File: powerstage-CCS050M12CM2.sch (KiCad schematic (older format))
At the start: 47 parts, among them Q2 CCS050M12CM2, U10 74LVC2G04, U11 TXS0108E

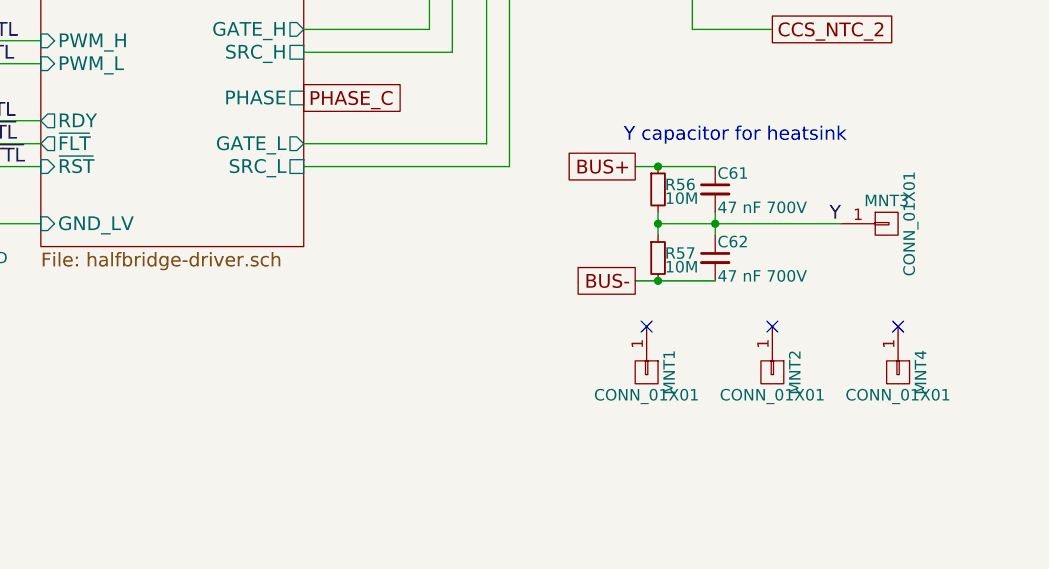
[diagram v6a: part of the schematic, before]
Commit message: YCAPS: Add real safety caps, dual Res
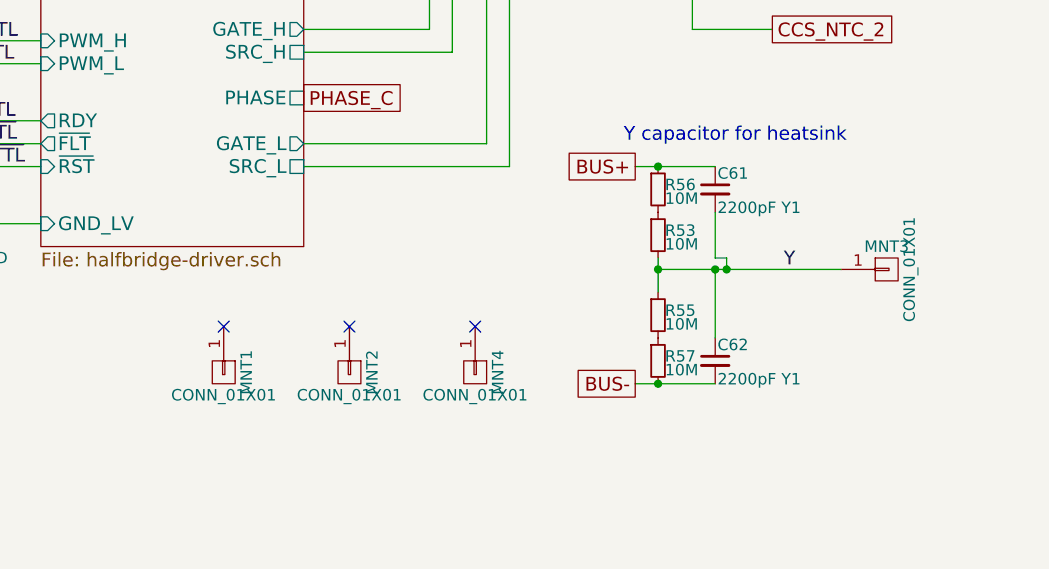
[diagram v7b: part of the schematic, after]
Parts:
- added R53, R55: 10M, Resistors_SMD:R_0805, symbol R_Small
- C61, C62: value 47 nF 700V -> 2200pF Y1; footprint Capacitors_SMD:C_1210 -> sictroller:CAP_ERP610_12-5MM; MPN (none) -> ERP610W222MERU
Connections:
- net Y: now also R53.2, R55.1; no longer R56.2, R57.1
- new net: R53.1, R56.2
- new net: R55.2, R57.1
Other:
- moved on the sheet: C62, MNT1, MNT2, MNT3, MNT4, R57
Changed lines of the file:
@@
 $EndDescr
 $Comp
-L +5VD #PWR116
+L +5VD #PWR0112
 U 1 1 57A1909B
 P 4150 4250
-F 0 "#PWR116" H 4150 4100 50  0001 C CNN
+F 0 "#PWR0112" H 4150 4100 50  0001 C CNN
 F 1 "+5VD" H 4150 4390 50  0000 C CNN
 F 2 "" H 4150 4250 50  0000 C CNN
@@
 $EndComp
 $Comp
-L GNDD #PWR111
+L GNDD #PWR0113
 U 1 1 57A19106
 P 2950 4550
-F 0 "#PWR111" H 2950 4300 50  0001 C CNN
+F 0 "#PWR0113" H 2950 4300 50  0001 C CNN
 F 1 "GNDD" H 2950 4400 50  0000 C CNN
 F 2 "" H 2950 4550 50  0000 C CNN
@@
 $EndComp
 $Comp
-L GNDD #PWR117
+L GNDD #PWR0114
 U 1 1 57A1910C
 P 4300 4550
-F 0 "#PWR117" H 4300 4300 50  0001 C CNN
+F 0 "#PWR0114" H 4300 4300 50  0001 C CNN
 F 1 "GNDD" H 4300 4400 50  0000 C CNN
 F 2 "" H 4300 4550 50  0000 C CNN
@@
 $EndComp
 $Comp
-L GNDD #PWR114
+L GNDD #PWR0115
 U 1 1 57A19193
 P 3250 5950
-F 0 "#PWR114" H 3250 5700 50  0001 C CNN
+F 0 "#PWR0115" H 3250 5700 50  0001 C CNN
 F 1 "GNDD" H 3250 5800 50  0000 C CNN
 F 2 "" H 3250 5950 50  0000 C CNN
@@
 $EndComp
 $Comp
-L +3.3V #PWR113
+L +3.3V #PWR0116
 U 1 1 57A19100
 P 3250 4250
-F 0 "#PWR113" H 3250 4100 50  0001 C CNN
+F 0 "#PWR0116" H 3250 4100 50  0001 C CNN
 F 1 "+3.3V" H 3250 4390 50  0000 C CNN
 F 2 "" H 3250 4250 50  0000 C CNN
@@
 $EndComp
 $Comp
-L GNDD #PWR108
+L GNDD #PWR0117
 U 1 1 57A23C37
 P 2200 2150
-F 0 "#PWR108" H 2200 1900 50  0001 C CNN
+F 0 "#PWR0117" H 2200 1900 50  0001 C CNN
 F 1 "GNDD" H 2200 2000 50  0000 C CNN
 F 2 "" H 2200 2150 50  0000 C CNN
@@
 $EndComp
 $Comp
-L +3.3V #PWR107
+L +3.3V #PWR0118
 U 1 1 57A23E25
 P 2200 1200
-F 0 "#PWR107" H 2200 1050 50  0001 C CNN
+F 0 "#PWR0118" H 2200 1050 50  0001 C CNN
 F 1 "+3.3V" H 2200 1340 50  0000 C CNN
 F 2 "" H 2200 1200 50  0000 C CNN
@@
 $EndComp
 $Comp
-L GNDD #PWR109
+L GNDD #PWR0119
 U 1 1 57A244F4
 P 2500 1450
-F 0 "#PWR109" H 2500 1200 50  0001 C CNN
+F 0 "#PWR0119" H 2500 1200 50  0001 C CNN
 F 1 "GNDD" H 2500 1300 50  0000 C CNN
 F 2 "" H 2500 1450 50  0000 C CNN
@@
 GDRV_RDY_TTL
 $Comp
-L +5VD #PWR122
+L +5VD #PWR0120
 U 1 1 57F46580
 P 5900 4750
-F 0 "#PWR122" H 5900 4600 50  0001 C CNN
+F 0 "#PWR0120" H 5900 4600 50  0001 C CNN
 F 1 "+5VD" H 5900 4890 50  0000 C CNN
 F 2 "" H 5900 4750 50  0000 C CNN
@@
 $EndComp
 $Comp
-L GNDD #PWR123
+L GNDD #PWR0121
 U 1 1 57F47836
 P 5900 5900
-F 0 "#PWR123" H 5900 5650 50  0001 C CNN
+F 0 "#PWR0121" H 5900 5650 50  0001 C CNN
 F 1 "GNDD" H 5900 5750 50  0000 C CNN
 F 2 "" H 5900 5900 50  0000 C CNN
@@
 $EndComp
 $Comp
-L GNDD #PWR121
+L GNDD #PWR0122
 U 1 1 57F48803
 P 5900 4000
-F 0 "#PWR121" H 5900 3750 50  0001 C CNN
+F 0 "#PWR0122" H 5900 3750 50  0001 C CNN
 F 1 "GNDD" H 5900 3850 50  0000 C CNN
 F 2 "" H 5900 4000 50  0000 C CNN
@@
 $EndComp
 $Comp
-L GNDD #PWR119
+L GNDD #PWR0123
 U 1 1 57F497CA
 P 5900 2100
-F 0 "#PWR119" H 5900 1850 50  0001 C CNN
+F 0 "#PWR0123" H 5900 1850 50  0001 C CNN
 F 1 "GNDD" H 5900 1950 50  0000 C CNN
 F 2 "" H 5900 2100 50  0000 C CNN
@@
 $EndComp
 $Comp
-L +5VD #PWR120
+L +5VD #PWR0124
 U 1 1 57F4B3DF
 P 5900 2850
-F 0 "#PWR120" H 5900 2700 50  0001 C CNN
+F 0 "#PWR0124" H 5900 2700 50  0001 C CNN
 F 1 "+5VD" H 5900 2990 50  0000 C CNN
 F 2 "" H 5900 2850 50  0000 C CNN
@@
 $EndComp
 $Comp
-L +5VD #PWR118
+L +5VD #PWR0125
 U 1 1 57F4C376
 P 5900 950
-F 0 "#PWR118" H 5900 800 50  0001 C CNN
+F 0 "#PWR0125" H 5900 800 50  0001 C CNN
 F 1 "+5VD" H 5900 1090 50  0000 C CNN
 F 2 "" H 5900 950 50  0000 C CNN
@@
 $EndComp
 $Comp
-L GNDD #PWR110
+L GNDD #PWR0126
 U 1 1 57F6D098
 P 2600 5950
-F 0 "#PWR110" H 2600 5700 50  0001 C CNN
+F 0 "#PWR0126" H 2600 5700 50  0001 C CNN
 F 1 "GNDD" H 2600 5800 50  0000 C CNN
 F 2 "" H 2600 5950 50  0000 C CNN
@@
 Text GLabel 8750 5650 0    60   UnSpc ~ 0
 BUS+
-Text GLabel 8750 6150 0    60   UnSpc ~ 0
+Text GLabel 8750 6600 0    60   UnSpc ~ 0
 BUS-
 $Comp
@@
 P 9100 5750
 F 0 "C61" H 9110 5820 50  0000 L CNN
-F 1 "47 nF 700V" H 9110 5670 50  0000 L CNN
-F 2 "Capacitors_SMD:C_1210" H 9100 5750 50  0001 C CNN
+F 1 "2200pF Y1" H 9110 5670 50  0000 L CNN
+F 2 "sictroller:CAP_ERP610_12-5MM" H 9100 5750 50  0001 C CNN
 F 3 "" H 9100 5750 50  0000 C CNN
+F 4 "ERP610W222MERU" H 9100 5750 60  0001 C CNN "MPN"
 	1    9100 5750
 	1    0    0    -1
@@
 L C_Small C62
 U 1 1 57FDCDC0
-P 9100 6050
-F 0 "C62" H 9110 6120 50  0000 L CNN
-F 1 "47 nF 700V" H 9110 5970 50  0000 L CNN
-F 2 "Capacitors_SMD:C_1210" H 9100 6050 50  0001 C CNN
-F 3 "" H 9100 6050 50  0000 C CNN
-	1    9100 6050
+P 9100 6500
+F 0 "C62" H 9110 6570 50  0000 L CNN
+F 1 "2200pF Y1" H 9110 6420 50  0000 L CNN
+F 2 "sictroller:CAP_ERP610_12-5MM" H 9100 6500 50  0001 C CNN
+F 3 "" H 9100 6500 50  0000 C CNN
+F 4 "ERP610W222MERU" H 9100 6500 60  0001 C CNN "MPN"
+	1    9100 6500
 	1    0    0    -1
 $EndComp
@@
 L R_Small R57
 U 1 1 57FDDE6B
-P 8850 6050
-F 0 "R57" H 8880 6070 50  0000 L CNN
-F 1 "10M" H 8880 6010 50  0000 L CNN
-F 2 "Resistors_SMD:R_0805" H 8850 6050 50  0001 C CNN
-F 3 "" H 8850 6050 50  0000 C CNN
-	1    8850 6050
+P 8850 6500
+F 0 "R57" H 8880 6520 50  0000 L CNN
+F 1 "10M" H 8880 6460 50  0000 L CNN
+F 2 "Resistors_SMD:R_0805" H 8850 6500 50  0001 C CNN
+F 3 "" H 8850 6500 50  0000 C CNN
+	1    8850 6500
 	1    0    0    -1
 $EndComp
@@
 L CONN_01X01 MNT3
 U 1 1 57FE17BD
-P 9850 5900
-F 0 "MNT3" H 9850 6000 50  0000 C CNN
-F 1 "CONN_01X01" V 9950 5900 50  0000 C CNN
-F 2 "sictroller:MountingHole_3mm_Pad_Via" H 9850 5900 50  0001 C CNN
-F 3 "" H 9850 5900 50  0000 C CNN
-	1    9850 5900
+P 9850 6100
+F 0 "MNT3" H 9850 6200 50  0000 C CNN
+F 1 "CONN_01X01" V 9950 6100 50  0000 C CNN
+F 2 "sictroller:MountingHole_3mm_Pad_Via" H 9850 6100 50  0001 C CNN
+F 3 "" H 9850 6100 50  0000 C CNN
+	1    9850 6100
 	1    0    0    -1
 $EndComp
@@
 $EndComp
 $Comp
-L +3.3V #PWR112
+L +3.3V #PWR0127
 U 1 1 5800C8BD
 P 3100 5650
-F 0 "#PWR112" H 3100 5500 50  0001 C CNN
+F 0 "#PWR0127" H 3100 5500 50  0001 C CNN
 F 1 "+3.3V" H 3100 5790 50  0000 C CNN
 F 2 "" H 3100 5650 50  0000 C CNN
@@
 	9000 5050 9000 4700
 Wire Wire Line
-	9100 5850 9100 5950
-Wire Wire Line
-	8850 5850 8850 5950
-Wire Wire Line
-	8850 5900 9650 5900
-Connection ~ 9100 5900
-Connection ~ 8850 5900
-Wire Wire Line
 	8750 5650 9100 5650
 Connection ~ 8850 5650
 Wire Wire Line
-	8750 6150 9100 6150
-Connection ~ 8850 6150
+	8750 6600 9100 6600
+Connection ~ 8850 6600
 Wire Wire Line
 	3250 4250 3250 4550
-Text Label 9600 5900 0    60   ~ 0
+Text Label 9400 6100 0    60   ~ 0
 Y
 Wire Wire Line
@@
 L CONN_01X01 MNT1
 U 1 1 580494E3
-P 8800 6550
-F 0 "MNT1" H 8800 6650 50  0000 C CNN
-F 1 "CONN_01X01" V 8900 6550 50  0000 C CNN
-F 2 "sictroller:MountingHole_3mm_Pad_Via" H 8800 6550 50  0001 C CNN
-F 3 "" H 8800 6550 50  0000 C CNN
-	1    8800 6550
+P 6950 6550
+F 0 "MNT1" H 6950 6650 50  0000 C CNN
+F 1 "CONN_01X01" V 7050 6550 50  0000 C CNN
+F 2 "sictroller:MountingHole_3mm_Pad_Via" H 6950 6550 50  0001 C CNN
+F 3 "" H 6950 6550 50  0000 C CNN
+	1    6950 6550
 	0    1    1    0
 $EndComp
@@
 L CONN_01X01 MNT2
 U 1 1 5804A0FB
-P 9350 6550
-F 0 "MNT2" H 9350 6650 50  0000 C CNN
-F 1 "CONN_01X01" V 9450 6550 50  0000 C CNN
-F 2 "sictroller:MountingHole_3mm_Pad_Via" H 9350 6550 50  0001 C CNN
-F 3 "" H 9350 6550 50  0000 C CNN
-	1    9350 6550
+P 7500 6550
+F 0 "MNT2" H 7500 6650 50  0000 C CNN
+F 1 "CONN_01X01" V 7600 6550 50  0000 C CNN
+F 2 "sictroller:MountingHole_3mm_Pad_Via" H 7500 6550 50  0001 C CNN
+F 3 "" H 7500 6550 50  0000 C CNN
+	1    7500 6550
 	0    1    1    0
 $EndComp
@@
 L CONN_01X01 MNT4
 U 1 1 5804A292
-P 9900 6550
-F 0 "MNT4" H 9900 6650 50  0000 C CNN
-F 1 "CONN_01X01" V 10000 6550 50  0000 C CNN
-F 2 "sictroller:MountingHole_3mm_Pad_Via" H 9900 6550 50  0001 C CNN
-F 3 "" H 9900 6550 50  0000 C CNN
-	1    9900 6550
+P 8050 6550
+F 0 "MNT4" H 8050 6650 50  0000 C CNN
+F 1 "CONN_01X01" V 8150 6550 50  0000 C CNN
+F 2 "sictroller:MountingHole_3mm_Pad_Via" H 8050 6550 50  0001 C CNN
+F 3 "" H 8050 6550 50  0000 C CNN
+	1    8050 6550
 	0    1    1    0
 $EndComp
-NoConn ~ 9900 6350
-NoConn ~ 9350 6350
-NoConn ~ 8800 6350
+NoConn ~ 8050 6350
+NoConn ~ 7500 6350
+NoConn ~ 6950 6350
 $Comp
 L R_Small R49
@@
 	2700 1950 2800 1950
 $Comp
-L GNDD #PWR115
+L GNDD #PWR0128
 U 1 1 58437DDD
 P 3525 2300
-F 0 "#PWR115" H 3525 2050 50  0001 C CNN
+F 0 "#PWR0128" H 3525 2050 50  0001 C CNN
 F 1 "GNDD" H 3525 2150 50  0000 C CNN
 F 2 "" H 3525 2300 50  0000 C CNN
@@
 Wire Wire Line
 	2700 2300 2700 1950
+$Comp
+L R_Small R53
+U 1 1 58CB1F67
+P 8850 5950
+F 0 "R53" H 8880 5970 50  0000 L CNN
+F 1 "10M" H 8880 5910 50  0000 L CNN
+F 2 "Resistors_SMD:R_0805" H 8850 5950 50  0001 C CNN
+F 3 "" H 8850 5950 50  0000 C CNN
+	1    8850 5950
+	1    0    0    -1
+$EndComp
+$Comp
+L R_Small R55
+U 1 1 58CB21C0
+P 8850 6300
+F 0 "R55" H 8880 6320 50  0000 L CNN
+F 1 "10M" H 8880 6260 50  0000 L CNN
+F 2 "Resistors_SMD:R_0805" H 8850 6300 50  0001 C CNN
+F 3 "" H 8850 6300 50  0000 C CNN
+	1    8850 6300
+	1    0    0    -1
+$EndComp
+Wire Wire Line
+	8850 6050 8850 6200
+Wire Wire Line
+	9650 6100 8850 6100
+Connection ~ 8850 6100
+Wire Wire Line
+	9100 6400 9100 6100
+Connection ~ 9100 6100
+Wire Wire Line
+	9100 5850 9100 6050
+Wire Wire Line
+	9100 6050 9150 6050
+Wire Wire Line
+	9150 6050 9150 6100
+Connection ~ 9150 6100
 $EndSCHEMATC

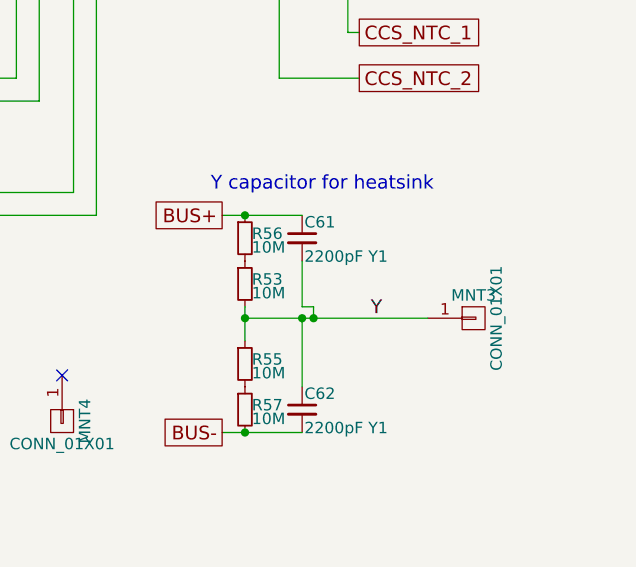
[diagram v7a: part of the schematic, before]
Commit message: WIP: Passes DRC. Need to remove fuse and merge gnd
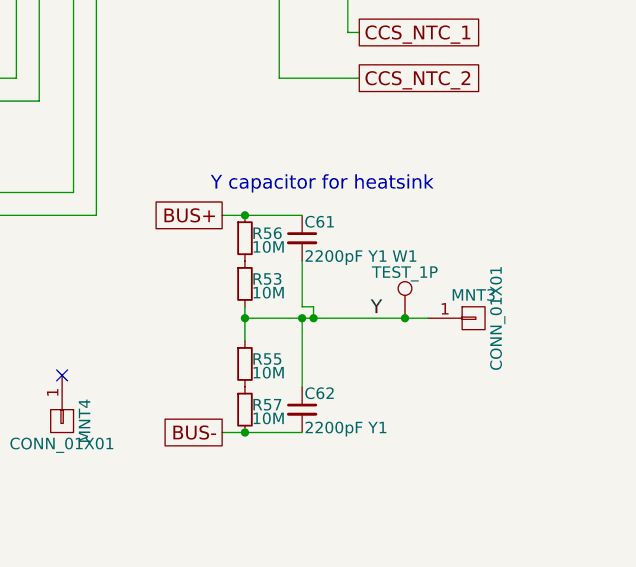
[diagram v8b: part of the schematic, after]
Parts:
- added W1: TEST_1P, Measurement_Points:Measurement_Point_Round-TH_Big, symbol TEST_1P
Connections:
- net Y: now also W1.1
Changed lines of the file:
@@
 $EndDescr
 $Comp
-L +5VD #PWR0112
+L +5VD #PWR0111
 U 1 1 57A1909B
 P 4150 4250
-F 0 "#PWR0112" H 4150 4100 50  0001 C CNN
+F 0 "#PWR0111" H 4150 4100 50  0001 C CNN
 F 1 "+5VD" H 4150 4390 50  0000 C CNN
 F 2 "" H 4150 4250 50  0000 C CNN
@@
 $EndComp
 $Comp
-L GNDD #PWR0113
+L GNDD #PWR0112
 U 1 1 57A19106
 P 2950 4550
-F 0 "#PWR0113" H 2950 4300 50  0001 C CNN
+F 0 "#PWR0112" H 2950 4300 50  0001 C CNN
 F 1 "GNDD" H 2950 4400 50  0000 C CNN
 F 2 "" H 2950 4550 50  0000 C CNN
@@
 $EndComp
 $Comp
-L GNDD #PWR0114
+L GNDD #PWR0113
 U 1 1 57A1910C
 P 4300 4550
-F 0 "#PWR0114" H 4300 4300 50  0001 C CNN
+F 0 "#PWR0113" H 4300 4300 50  0001 C CNN
 F 1 "GNDD" H 4300 4400 50  0000 C CNN
 F 2 "" H 4300 4550 50  0000 C CNN
@@
 $EndComp
 $Comp
-L GNDD #PWR0115
+L GNDD #PWR0114
 U 1 1 57A19193
 P 3250 5950
-F 0 "#PWR0115" H 3250 5700 50  0001 C CNN
+F 0 "#PWR0114" H 3250 5700 50  0001 C CNN
 F 1 "GNDD" H 3250 5800 50  0000 C CNN
 F 2 "" H 3250 5950 50  0000 C CNN
@@
 $EndComp
 $Comp
-L +3.3V #PWR0116
+L +3.3V #PWR0115
 U 1 1 57A19100
 P 3250 4250
-F 0 "#PWR0116" H 3250 4100 50  0001 C CNN
+F 0 "#PWR0115" H 3250 4100 50  0001 C CNN
 F 1 "+3.3V" H 3250 4390 50  0000 C CNN
 F 2 "" H 3250 4250 50  0000 C CNN
@@
 $EndComp
 $Comp
-L GNDD #PWR0117
+L GNDD #PWR0116
 U 1 1 57A23C37
 P 2200 2150
-F 0 "#PWR0117" H 2200 1900 50  0001 C CNN
+F 0 "#PWR0116" H 2200 1900 50  0001 C CNN
 F 1 "GNDD" H 2200 2000 50  0000 C CNN
 F 2 "" H 2200 2150 50  0000 C CNN
@@
 $EndComp
 $Comp
-L +3.3V #PWR0118
+L +3.3V #PWR0117
 U 1 1 57A23E25
 P 2200 1200
-F 0 "#PWR0118" H 2200 1050 50  0001 C CNN
+F 0 "#PWR0117" H 2200 1050 50  0001 C CNN
 F 1 "+3.3V" H 2200 1340 50  0000 C CNN
 F 2 "" H 2200 1200 50  0000 C CNN
@@
 $EndComp
 $Comp
-L GNDD #PWR0119
+L GNDD #PWR0118
 U 1 1 57A244F4
 P 2500 1450
-F 0 "#PWR0119" H 2500 1200 50  0001 C CNN
+F 0 "#PWR0118" H 2500 1200 50  0001 C CNN
 F 1 "GNDD" H 2500 1300 50  0000 C CNN
 F 2 "" H 2500 1450 50  0000 C CNN
@@
 GDRV_RDY_TTL
 $Comp
-L +5VD #PWR0120
+L +5VD #PWR0119
 U 1 1 57F46580
 P 5900 4750
-F 0 "#PWR0120" H 5900 4600 50  0001 C CNN
+F 0 "#PWR0119" H 5900 4600 50  0001 C CNN
 F 1 "+5VD" H 5900 4890 50  0000 C CNN
 F 2 "" H 5900 4750 50  0000 C CNN
@@
 $EndComp
 $Comp
-L GNDD #PWR0121
+L GNDD #PWR0120
 U 1 1 57F47836
 P 5900 5900
-F 0 "#PWR0121" H 5900 5650 50  0001 C CNN
+F 0 "#PWR0120" H 5900 5650 50  0001 C CNN
 F 1 "GNDD" H 5900 5750 50  0000 C CNN
 F 2 "" H 5900 5900 50  0000 C CNN
@@
 $EndComp
 $Comp
-L GNDD #PWR0122
+L GNDD #PWR0121
 U 1 1 57F48803
 P 5900 4000
-F 0 "#PWR0122" H 5900 3750 50  0001 C CNN
+F 0 "#PWR0121" H 5900 3750 50  0001 C CNN
 F 1 "GNDD" H 5900 3850 50  0000 C CNN
 F 2 "" H 5900 4000 50  0000 C CNN
@@
 $EndComp
 $Comp
-L GNDD #PWR0123
+L GNDD #PWR0122
 U 1 1 57F497CA
 P 5900 2100
-F 0 "#PWR0123" H 5900 1850 50  0001 C CNN
+F 0 "#PWR0122" H 5900 1850 50  0001 C CNN
 F 1 "GNDD" H 5900 1950 50  0000 C CNN
 F 2 "" H 5900 2100 50  0000 C CNN
@@
 $EndComp
 $Comp
-L +5VD #PWR0124
+L +5VD #PWR0123
 U 1 1 57F4B3DF
 P 5900 2850
-F 0 "#PWR0124" H 5900 2700 50  0001 C CNN
+F 0 "#PWR0123" H 5900 2700 50  0001 C CNN
 F 1 "+5VD" H 5900 2990 50  0000 C CNN
 F 2 "" H 5900 2850 50  0000 C CNN
@@
 $EndComp
 $Comp
-L +5VD #PWR0125
+L +5VD #PWR0124
 U 1 1 57F4C376
 P 5900 950
-F 0 "#PWR0125" H 5900 800 50  0001 C CNN
+F 0 "#PWR0124" H 5900 800 50  0001 C CNN
 F 1 "+5VD" H 5900 1090 50  0000 C CNN
 F 2 "" H 5900 950 50  0000 C CNN
@@
 $EndComp
 $Comp
-L GNDD #PWR0126
+L GNDD #PWR0125
 U 1 1 57F6D098
 P 2600 5950
-F 0 "#PWR0126" H 2600 5700 50  0001 C CNN
+F 0 "#PWR0125" H 2600 5700 50  0001 C CNN
 F 1 "GNDD" H 2600 5800 50  0000 C CNN
 F 2 "" H 2600 5950 50  0000 C CNN
@@
 $EndComp
 $Comp
-L +3.3V #PWR0127
+L +3.3V #PWR0126
 U 1 1 5800C8BD
 P 3100 5650
-F 0 "#PWR0127" H 3100 5500 50  0001 C CNN
+F 0 "#PWR0126" H 3100 5500 50  0001 C CNN
 F 1 "+3.3V" H 3100 5790 50  0000 C CNN
 F 2 "" H 3100 5650 50  0000 C CNN
@@
 	2700 1950 2800 1950
 $Comp
-L GNDD #PWR0128
+L GNDD #PWR0127
 U 1 1 58437DDD
 P 3525 2300
-F 0 "#PWR0128" H 3525 2050 50  0001 C CNN
+F 0 "#PWR0127" H 3525 2050 50  0001 C CNN
 F 1 "GNDD" H 3525 2150 50  0000 C CNN
 F 2 "" H 3525 2300 50  0000 C CNN
@@
 	9150 6050 9150 6100
 Connection ~ 9150 6100
+$Comp
+L TEST_1P W1
+U 1 1 58CF0503
+P 9550 6100
+F 0 "W1" H 9550 6370 50  0000 C CNN
+F 1 "TEST_1P" H 9550 6300 50  0000 C CNN
+F 2 "Measurement_Points:Measurement_Point_Round-TH_Big" H 9750 6100 50  0001 C CNN
+F 3 "" H 9750 6100 50  0000 C CNN
+	1    9550 6100
+	1    0    0    -1
+$EndComp
+Connection ~ 9550 6100
 $EndSCHEMATC
